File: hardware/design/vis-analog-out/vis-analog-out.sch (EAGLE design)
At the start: 6 parts, among them J1 FH12-8S-0.5SH(55), U1 Chromation-optical-die-in-QFN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

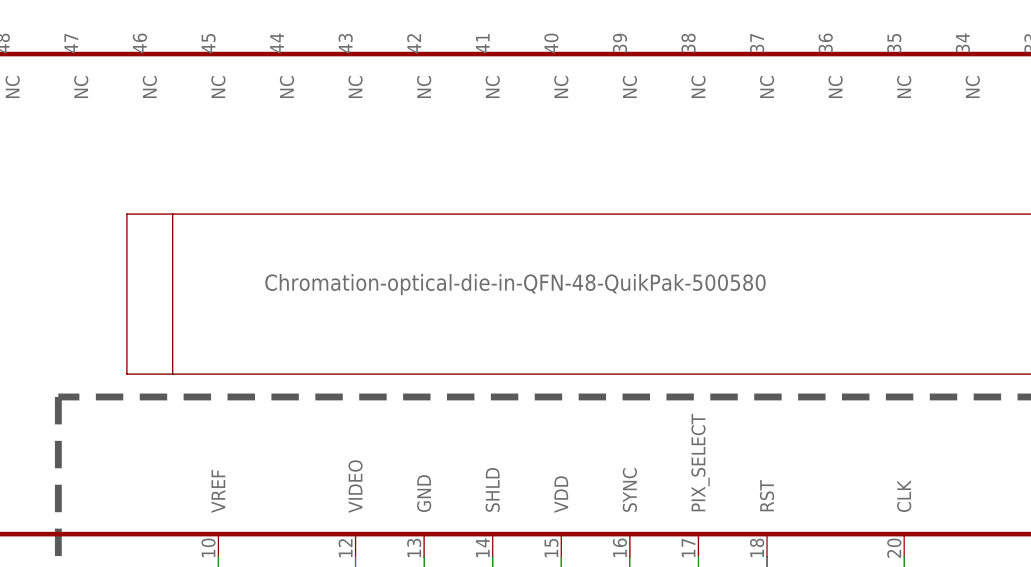
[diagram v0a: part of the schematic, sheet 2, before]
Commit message: Consolidate EAGLE libraries into hardware/design/lbr
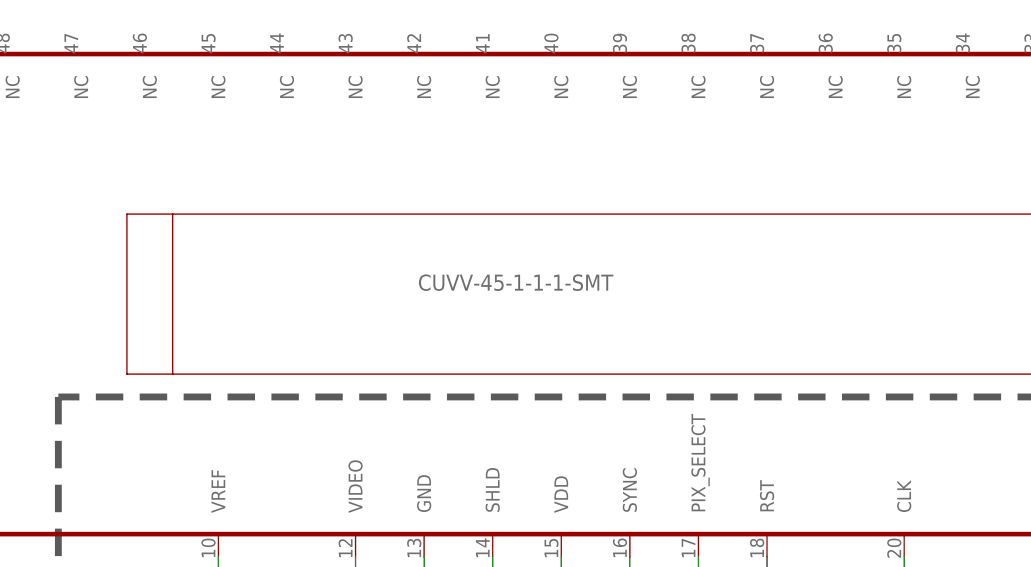
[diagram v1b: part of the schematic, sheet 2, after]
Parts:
- U1: value Chromation-optical-die-in-QFN-48-QuikPak-500580 -> CUVV-45-1-1-1-SMT; MANUF_PNUM Spectrometer -> CUVV-45-1-1-1-SMT; VENDOR1_PNUM Spectrometer -> CUVV-45-1-1-1-SMT
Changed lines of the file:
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@@
 <part name="FRAME1" library="Chromation" deviceset="LETTER_L" device="" value="frame1"/>
 <part name="FRAME2" library="Chromation" deviceset="LETTER_L" device="" value="frame2"/>
-<part name="U1" library="VIS-PKG" deviceset="VIS" device="-QFN48" override_package3d_urn="urn:adsk.eagle:package:12144447/8" override_package_urn="urn:adsk.eagle:footprint:12144448/2" value="Chromation-optical-die-in-QFN-48-QuikPak-500580">
+<part name="U1" library="VIS-PKG" deviceset="VIS" device="-QFN48" override_package3d_urn="urn:adsk.eagle:package:12144447/8" override_package_urn="urn:adsk.eagle:footprint:12144448/2" value="CUVV-45-1-1-1-SMT">
 <attribute name="EXPORT" value="YES"/>
 <attribute name="MANUF" value="Chromation"/>
-<attribute name="MANUF_PNUM" value="Spectrometer"/>
+<attribute name="MANUF_PNUM" value="CUVV-45-1-1-1-SMT"/>
 <attribute name="NOTES" value="--"/>
 <attribute name="VENDOR1" value="Chromation"/>
-<attribute name="VENDOR1_PNUM" value="Spectrometer"/>
+<attribute name="VENDOR1_PNUM" value="CUVV-45-1-1-1-SMT"/>
 <attribute name="VENDOR1_PQ_00001" value="--"/>
 </part>
